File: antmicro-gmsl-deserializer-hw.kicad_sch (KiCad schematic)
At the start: 6 parts

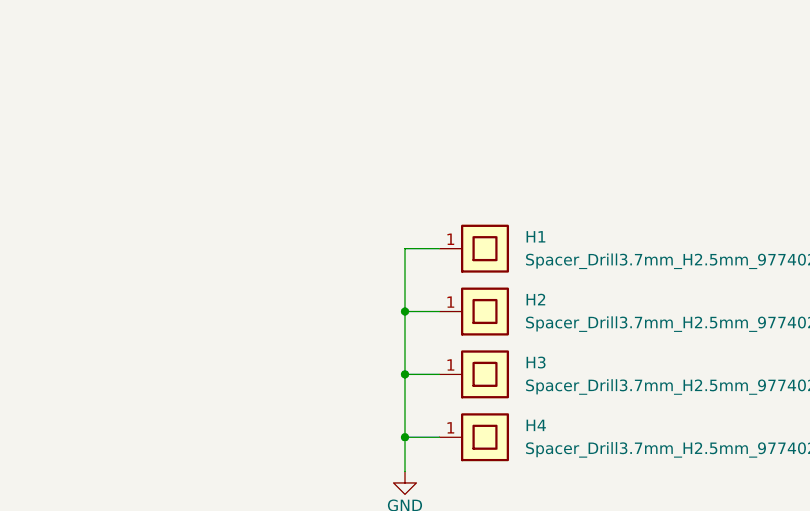
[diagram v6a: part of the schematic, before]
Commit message: Clean ERC, move LED from 5V to 12V
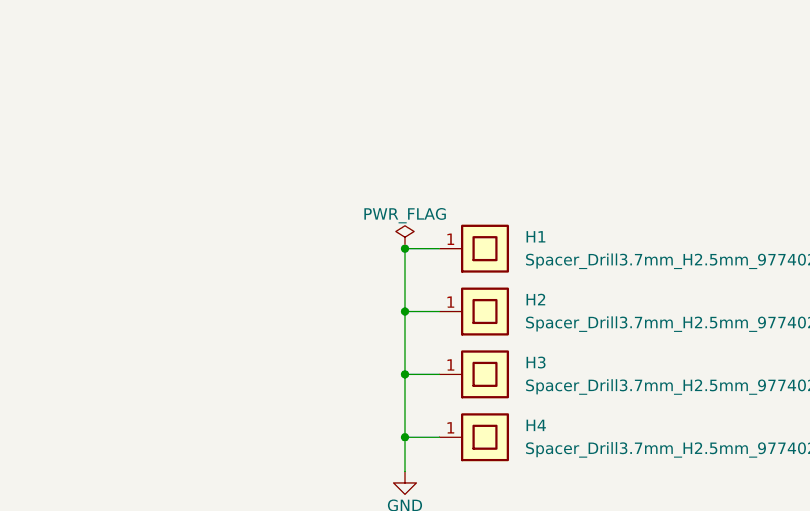
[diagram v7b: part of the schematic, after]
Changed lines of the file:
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@@
     (comment 1 "www.antmicro.com")
+  )
+  (junction (at 349.25 221.615) (diameter 0) (color 0 0 0 0)
   )
   (junction (at 349.25 242.57) (diameter 0) (color 0 0 0 0)
@@
     (pin "1")
   )
+  (symbol (lib_id "antmicropower:PWR_FLAG") (at 349.25 221.615 0) (unit 1)
+    (in_bom yes) (on_board yes)
+    (property "Reference" "#FLG0103" (id 0) (at 349.25 219.71 0)
+      (effects (font (size 1.27 1.27)) hide)
+    )
+    (property "Value" "PWR_FLAG" (id 1) (at 349.25 217.805 0))
+    (property "Footprint" "" (id 2) (at 349.25 221.615 0)
+      (effects (font (size 1.27 1.27)) hide)
+    )
+    (property "Datasheet" "" (id 3) (at 349.25 221.615 0)
+      (effects (font (size 1.27 1.27)) hide)
+    )
+    (pin "1")
+  )
   (sheet (at 88.9 198.755) (size 45.72 39.37) (fields_autoplaced)
     (stroke (width 0.1524) (type solid) (color 0 0 0 0))
@@
   )
   (symbol_instances
+    (path "/67434a8c-79b7-41fa-b4c4-5db7983eccb1/9b26a6ca-deab-4a2c-a750-4b996027ca22"
+      (reference "#FLG0101") (unit 1) (value "PWR_FLAG") (footprint "")
+    )
+    (path "/67434a8c-79b7-41fa-b4c4-5db7983eccb1/bf54b915-2d6c-4b8c-8c33-04eacb17362d"
+      (reference "#FLG0102") (unit 1) (value "PWR_FLAG") (footprint "")
+    )
+    (path "/db6f629c-c790-43b0-9f6f-5bc72cf8b596"
+      (reference "#FLG0103") (unit 1) (value "PWR_FLAG") (footprint "")
+    )
+    (path "/32fa9edb-d9f7-4795-8f8b-6c5ca11623b5/1f3092a0-a31a-451d-b86c-83b988bc8e0e"
+      (reference "#FLG0104") (unit 1) (value "PWR_FLAG") (footprint "")
+    )
+    (path "/32fa9edb-d9f7-4795-8f8b-6c5ca11623b5/28fa7cf7-85c2-499f-ae54-7b6f01de7df5"
+      (reference "#FLG0106") (unit 1) (value "PWR_FLAG") (footprint "")
+    )
+    (path "/32fa9edb-d9f7-4795-8f8b-6c5ca11623b5/c876aa33-dbb1-44a0-9568-b927653df70d"
+      (reference "#FLG0108") (unit 1) (value "PWR_FLAG") (footprint "")
+    )
     (path "/67434a8c-79b7-41fa-b4c4-5db7983eccb1/168eea42-ba70-4574-a447-d9144072f20d"
       (reference "#PWR01") (unit 1) (value "+1V8") (footprint "")
@@
       (reference "#PWR016") (unit 1) (value "GND") (footprint "")
     )
-    (path "/67434a8c-79b7-41fa-b4c4-5db7983eccb1/8077fe6e-8432-4029-8ce8-82821bf4aec4"
+    (path "/67434a8c-79b7-41fa-b4c4-5db7983eccb1/28b282df-bd08-45b0-8037-f957e1b865ee"
       (reference "#PWR017") (unit 1) (value "GND") (footprint "")
     )
@@
       (reference "#PWR059") (unit 1) (value "GND") (footprint "")
     )
-    (path "/32fa9edb-d9f7-4795-8f8b-6c5ca11623b5/ede063a0-bba1-4d3f-965f-28ebdb0fae62"
-      (reference "#PWR060") (unit 1) (value "+1V8") (footprint "")
-    )
     (path "/32fa9edb-d9f7-4795-8f8b-6c5ca11623b5/3baacc95-9cc5-4a6f-881d-c9fa598c756f"
       (reference "#PWR061") (unit 1) (value "+1V2") (footprint "")
@@
       (reference "#PWR0117") (unit 1) (value "GND") (footprint "")
     )
+    (path "/32fa9edb-d9f7-4795-8f8b-6c5ca11623b5/04eb3bd6-67d6-4f18-90cf-64ec64984856"
+      (reference "#PWR0118") (unit 1) (value "+1V8") (footprint "")
+    )
     (path "/67434a8c-79b7-41fa-b4c4-5db7983eccb1/297ffae4-44cd-4fea-9756-7c4f45405a0c"
       (reference "C1") (unit 1) (value "C_10u_25V_0603") (footprint "antmicro-footprints:C_0603_1608Metric")
@@
       (reference "D1") (unit 1) (value "SMF4L15A") (footprint "antmicro-footprints:SOD-123FL")
     )
-    (path "/67434a8c-79b7-41fa-b4c4-5db7983eccb1/34dad493-cb9d-4746-8896-aee9437a439c"
+    (path "/67434a8c-79b7-41fa-b4c4-5db7983eccb1/164b4950-c030-456a-99d4-8b645553765d"
       (reference "D2") (unit 1) (value "LED_G_0603_LTST-C190GKT") (footprint "antmicro-footprints:LED_0603_1608Metric_G")
     )
@@
       (reference "R6") (unit 1) (value "R_0R_0402") (footprint "antmicro-footprints:R_0402_1005Metric")
     )
-    (path "/67434a8c-79b7-41fa-b4c4-5db7983eccb1/da57c8f0-637a-4ffe-9ba8-05c56f172436"
+    (path "/67434a8c-79b7-41fa-b4c4-5db7983eccb1/ebf5b67d-5967-45a0-85d0-2d774f1b472f"
       (reference "R7") (unit 1) (value "R_470R_0402") (footprint "antmicro-footprints:R_0402_1005Metric")
     )

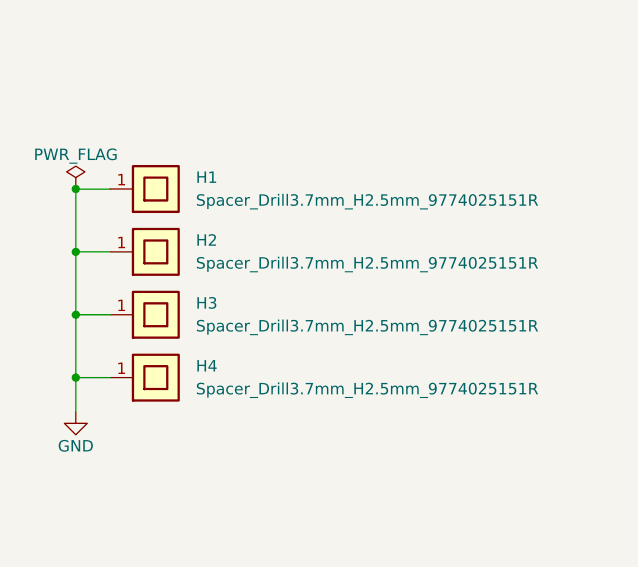
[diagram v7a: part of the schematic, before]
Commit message: Change standoffs
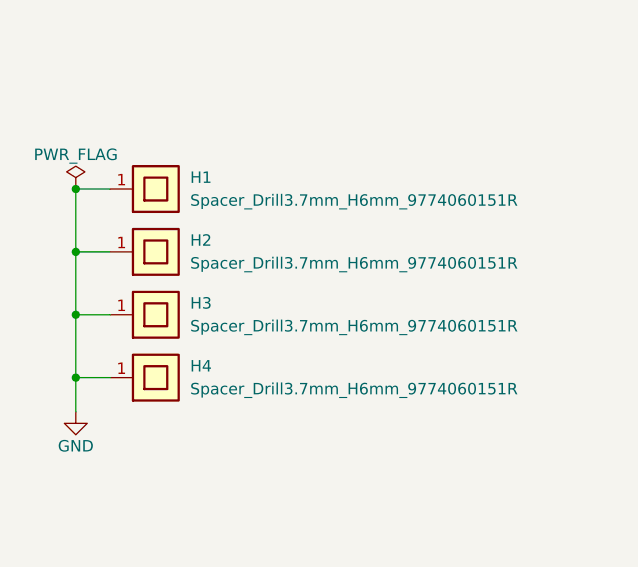
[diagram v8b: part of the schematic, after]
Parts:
- removed H1, H2, H3, H4: Spacer_Drill3.7mm_H2.5mm_9774025151R, antmicro-footprints:Spacer_Drill3.7mm_H2.5mm_9774025151R, symbol antmicroMechanicalParts:Spacer_Drill3.7mm_H2.5mm_9774025151R
- added H1, H2, H3, H4: Spacer_Drill3.7mm_H6mm_9774060151R, antmicro-footprints:Spacer_Drill3.7mm_H6mm_9774060151R, symbol antmicroMechanicalParts:Spacer_Drill3.7mm_H6mm_9774060151R
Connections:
- net GND: now also H1.1, H2.1, H3.1, H4.1
